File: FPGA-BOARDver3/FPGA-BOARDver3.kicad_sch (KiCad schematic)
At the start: 0 parts

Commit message: spdif fpga bansks
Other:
- added sheet FPGA Banks, Anti Alias Filters (FPGA_Banks_Anti_Alias_Filters.kicad_sch)
- added sheet SPDIF (SPDIF.kicad_sch)
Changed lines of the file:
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@@
 	(paper "A4")
+	(sheet
+		(at 59.69 97.79)
+		(size 20.32 26.67)
+		(fields_autoplaced yes)
+		(stroke
+			(width 0.1524)
+			(type solid)
+		)
+		(fill
+			(color 0 0 0 0.0000)
+		)
+		(property "Sheetname" "FPGA Banks, Anti Alias Filters"
+			(at 59.69 97.0784 0)
+			(effects
+				(font
+					(size 1.27 1.27)
+				)
+				(justify left bottom)
+			)
+		)
+		(property "Sheetfile" "FPGA_Banks_Anti_Alias_Filters.kicad_sch"
+			(at 59.69 125.0446 0)
+			(effects
+				(font
+					(size 1.27 1.27)
+				)
+				(justify left top)
+			)
+		)
+		(instances
+			(project "FPGA-BOARDver3"
+				(path "/4a327bdf-04e5-4836-9c0a-5fb801c23f64"
+					(page "8")
+				)
+			)
+		)
+	)
 	(sheet
 		(at 22.86 58.42)
@@
 				)
 			)
+		)
+	)
+	(sheet
+		(at 59.69 139.7)
+		(size 22.86 29.21)
+		(fields_autoplaced yes)
+		(stroke
+			(width 0.1524)
+			(type solid)
+		)
+		(fill
+			(color 0 0 0 0.0000)
+		)
+		(property "Sheetname" "SPDIF"
+			(at 59.69 138.9884 0)
+			(effects
+				(font
+					(size 1.27 1.27)
+				)
+				(justify left bottom)
+			)
+		)
+		(property "Sheetfile" "SPDIF.kicad_sch"
+			(at 59.69 169.4946 0)
+			(effects
+				(font
+					(size 1.27 1.27)
+				)
+				(justify left top)
+			)
+		)
+		(instances
+			(project "FPGA-BOARDver3"
+				(path "/4a327bdf-04e5-4836-9c0a-5fb801c23f64"
+					(page "9")
+				)
+			)

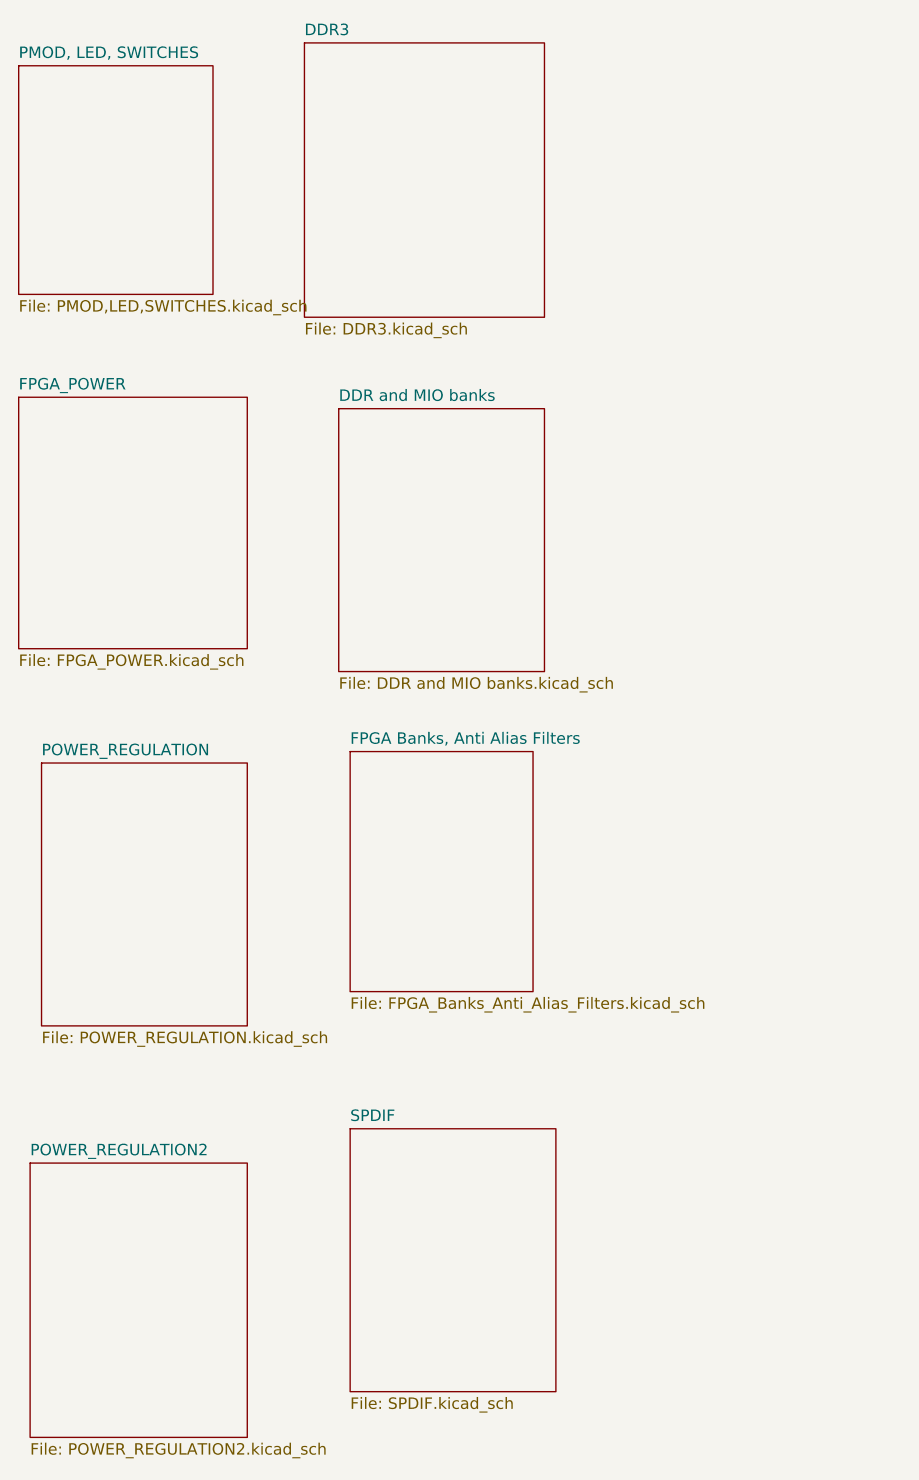
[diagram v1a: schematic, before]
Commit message: All pages complete , pi header left
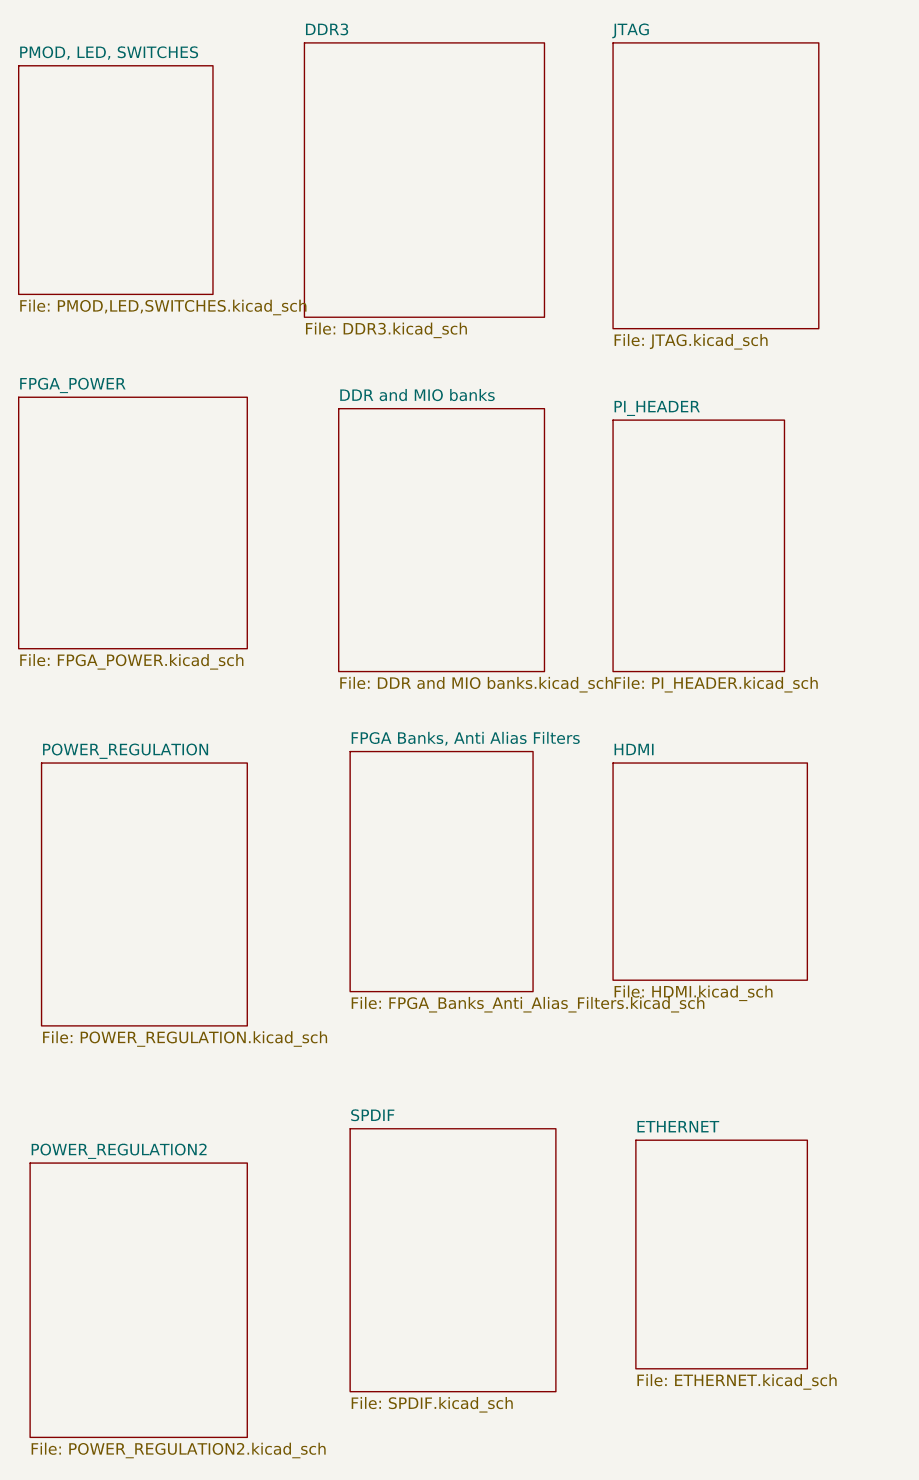
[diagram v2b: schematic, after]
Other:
- added sheet ETHERNET (ETHERNET.kicad_sch)
- added sheet HDMI (HDMI.kicad_sch)
- added sheet JTAG (JTAG.kicad_sch)
- added sheet PI_HEADER (PI_HEADER.kicad_sch)
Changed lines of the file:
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@@
 	(paper "A4")
+	(sheet
+		(at 91.44 140.97)
+		(size 19.05 25.4)
+		(fields_autoplaced yes)
+		(stroke
+			(width 0.1524)
+			(type solid)
+		)
+		(fill
+			(color 0 0 0 0.0000)
+		)
+		(property "Sheetname" "ETHERNET"
+			(at 91.44 140.2584 0)
+			(effects
+				(font
+					(size 1.27 1.27)
+				)
+				(justify left bottom)
+			)
+		)
+		(property "Sheetfile" "ETHERNET.kicad_sch"
+			(at 91.44 166.9546 0)
+			(effects
+				(font
+					(size 1.27 1.27)
+				)
+				(justify left top)
+			)
+		)
+		(instances
+			(project "FPGA-BOARDver3"
+				(path "/4a327bdf-04e5-4836-9c0a-5fb801c23f64"
+					(page "13")
+				)
+			)
+		)
+	)
 	(sheet
 		(at 59.69 97.79)
@@
 				)
 			)
+		)
+	)
+	(sheet
+		(at 88.9 19.05)
+		(size 22.86 31.75)
+		(fields_autoplaced yes)
+		(stroke
+			(width 0.1524)
+			(type solid)
+		)
+		(fill
+			(color 0 0 0 0.0000)
+		)
+		(property "Sheetname" "JTAG"
+			(at 88.9 18.3384 0)
+			(effects
+				(font
+					(size 1.27 1.27)
+				)
+				(justify left bottom)
+			)
+		)
+		(property "Sheetfile" "JTAG.kicad_sch"
+			(at 88.9 51.3846 0)
+			(effects
+				(font
+					(size 1.27 1.27)
+				)
+				(justify left top)
+			)
+		)
+		(instances
+			(project "FPGA-BOARDver3"
+				(path "/4a327bdf-04e5-4836-9c0a-5fb801c23f64"
+					(page "10")
+				)
+			)
+		)
+	)
+	(sheet
+		(at 88.9 99.06)
+		(size 21.59 24.13)
+		(fields_autoplaced yes)
+		(stroke
+			(width 0.1524)
+			(type solid)
+		)
+		(fill
+			(color 0 0 0 0.0000)
+		)
+		(property "Sheetname" "HDMI"
+			(at 88.9 98.3484 0)
+			(effects
+				(font
+					(size 1.27 1.27)
+				)
+				(justify left bottom)
+			)
+		)
+		(property "Sheetfile" "HDMI.kicad_sch"
+			(at 88.9 123.7746 0)
+			(effects
+				(font
+					(size 1.27 1.27)
+				)
+				(justify left top)
+			)
+		)
+		(instances
+			(project "FPGA-BOARDver3"
+				(path "/4a327bdf-04e5-4836-9c0a-5fb801c23f64"
+					(page "12")
+				)
+			)
+		)
+	)
+	(sheet
+		(at 88.9 60.96)
+		(size 19.05 27.94)
+		(fields_autoplaced yes)
+		(stroke
+			(width 0.1524)
+			(type solid)
+		)
+		(fill
+			(color 0 0 0 0.0000)
+		)
+		(property "Sheetname" "PI_HEADER"
+			(at 88.9 60.2484 0)
+			(effects
+				(font
+					(size 1.27 1.27)
+				)
+				(justify left bottom)
+			)
+		)
+		(property "Sheetfile" "PI_HEADER.kicad_sch"
+			(at 88.9 89.4846 0)
+			(effects
+				(font
+					(size 1.27 1.27)
+				)
+				(justify left top)
+			)
+		)
+		(instances
+			(project "FPGA-BOARDver3"
+				(path "/4a327bdf-04e5-4836-9c0a-5fb801c23f64"
+					(page "11")
+				)
+			)
